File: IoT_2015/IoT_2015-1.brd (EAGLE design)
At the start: 30 x 20 mm, 28 parts, among them Y1 ABLS-16.000MHZ-B4-T

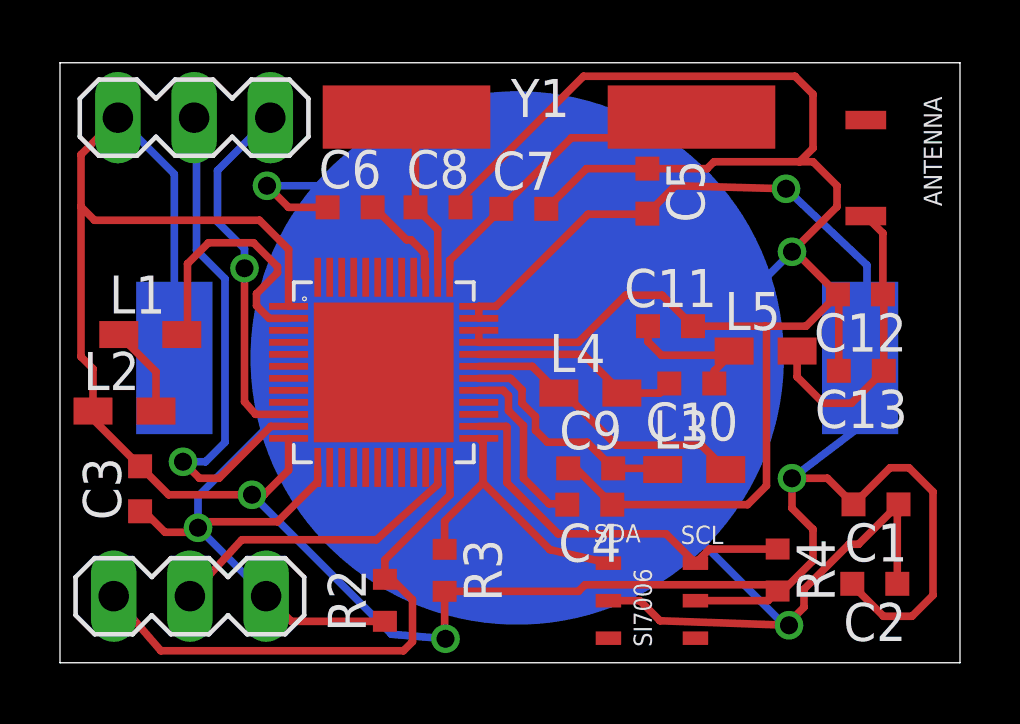
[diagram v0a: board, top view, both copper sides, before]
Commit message: Layout
Boardlayout is finished, the Gerberfile needs to be created.
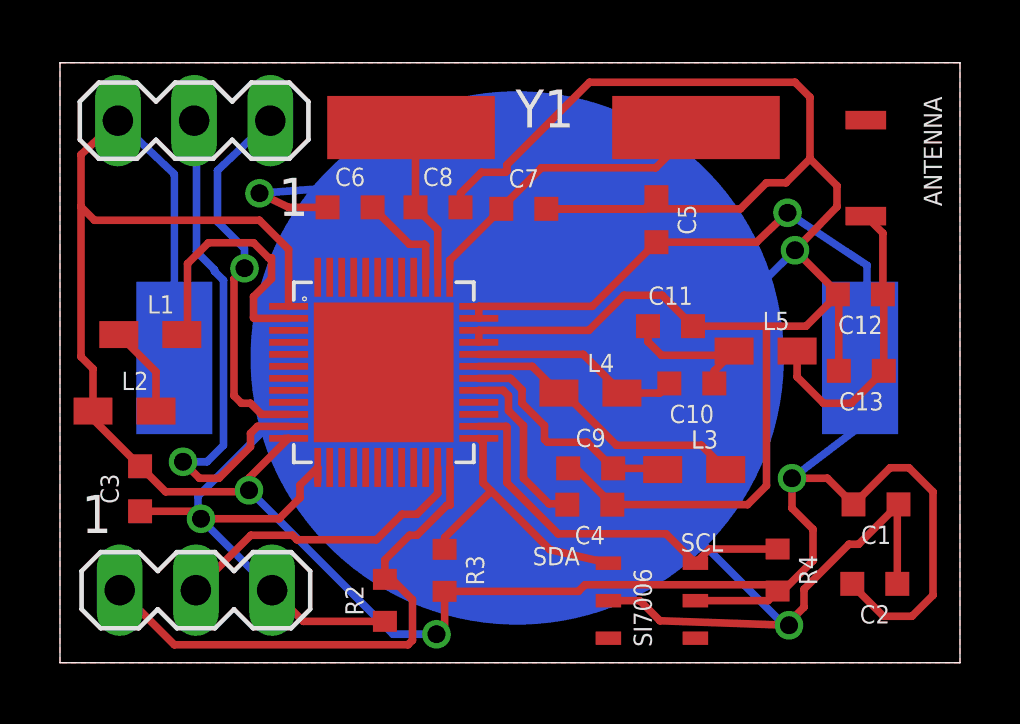
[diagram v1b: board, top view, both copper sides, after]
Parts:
- moved C5 1.00 mm to (19.9, 14.8)
- moved Y1 0.38 mm to (16.4, 17.8)
- moved JTAG 0.28 mm to (4.53, 2.42)
- moved P67VDD 0.10 mm to (4.47, 18.1)
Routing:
- net GND: track 141.4 -> 144.9 mm
- net VDD: track 105.2 -> 103.9 mm
- added copper zone on layer 1, net GND
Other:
- board text added: "CLK"
- board text added: "GND"
- board text added: "IO/NR"
- board text added: "JTAG"
- board text added: "P6"
- board text added: "P7"
- board text added: "VDD"
